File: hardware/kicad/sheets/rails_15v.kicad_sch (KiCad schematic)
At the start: 31 parts, among them U10 ADP7182AUJZ, U8 ADP5071AREZ, U9 ADP7142AUJZ

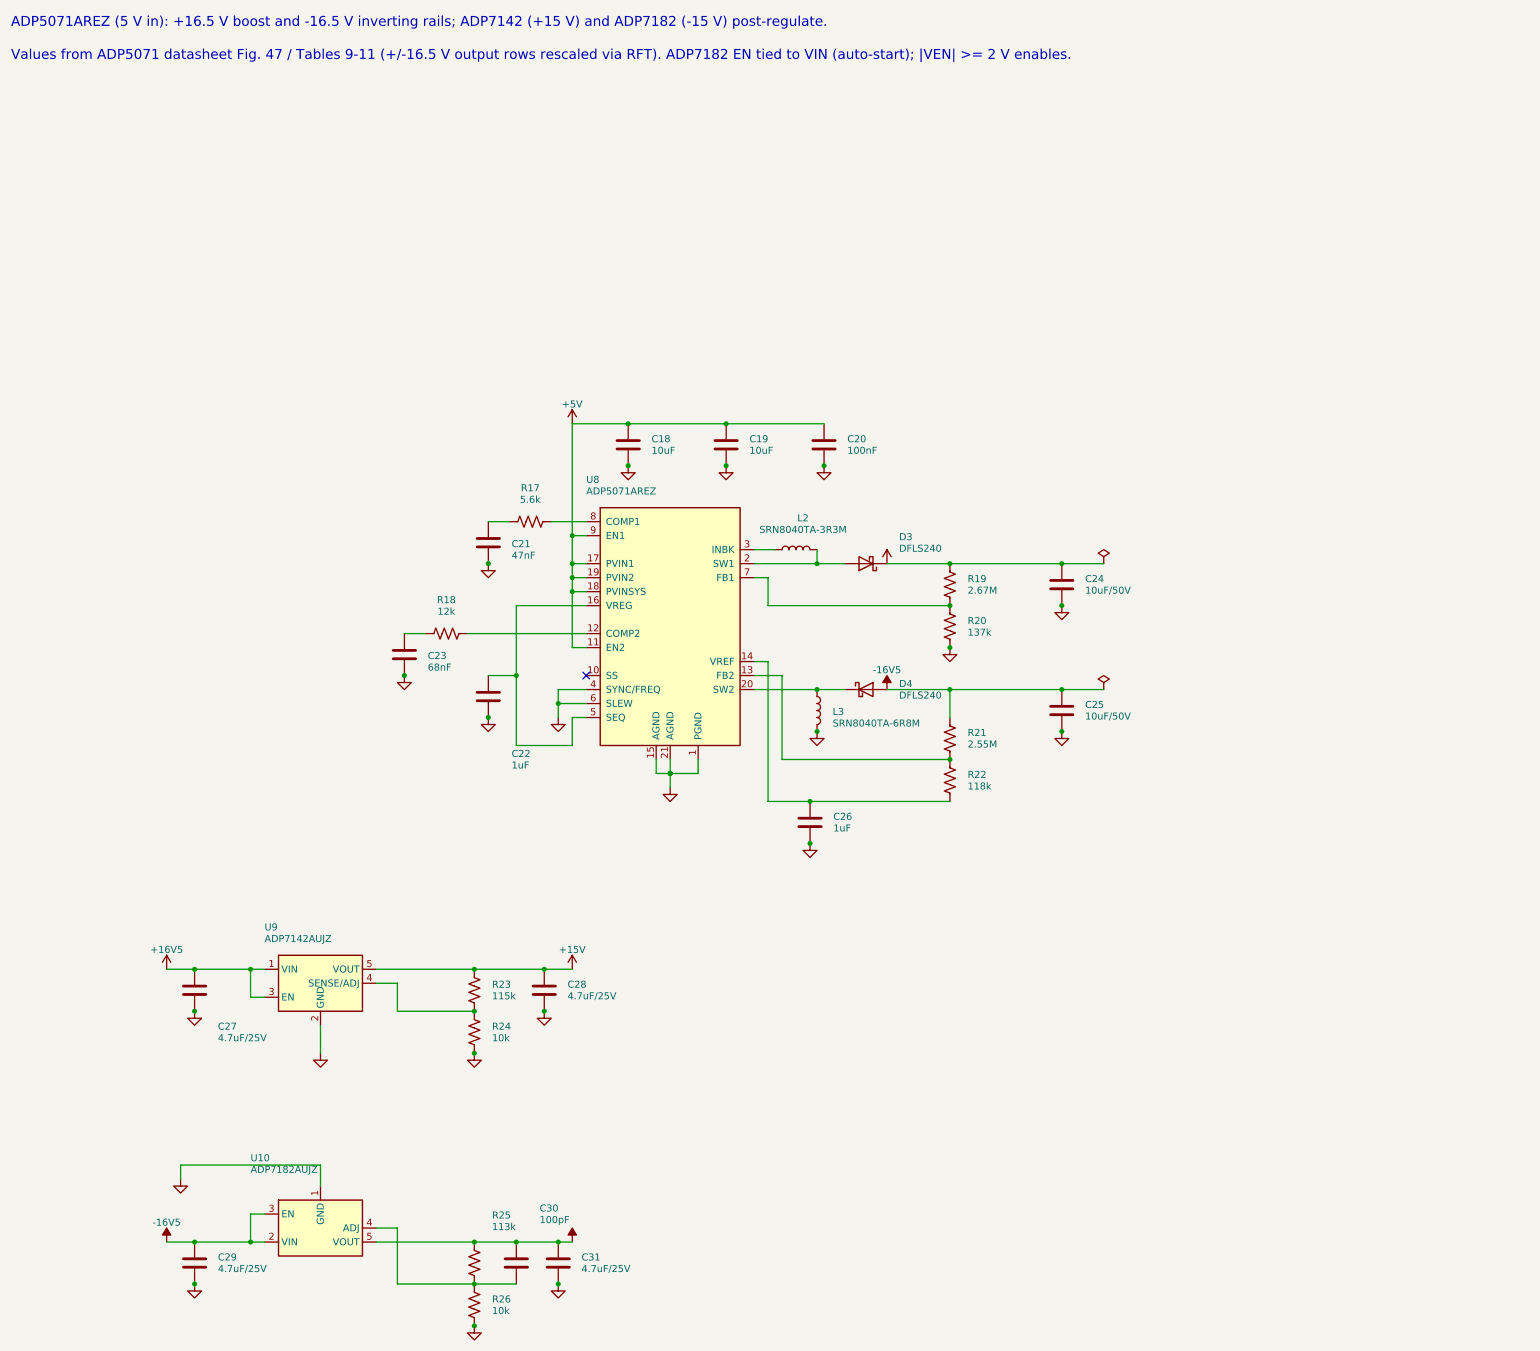
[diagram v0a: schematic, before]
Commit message: KiCad: cleaner layout, decoupling blocks, label directions, KiCad format fixes
- move IC decoupling caps into labelled blocks at the side of each sheet
- global labels show input/output direction per net
- no 4-way junctions (generator now checks and fails)
- generator output matches KiCad's saved format (hide property, junction
  and wire normalisation, lib symbol embedded fonts, multi-unit pins)
- hand-laid USB ESD protection as a pass-through

Co-Authored-By: Claude Sonnet 5.5 <noreply@anthropic.com>
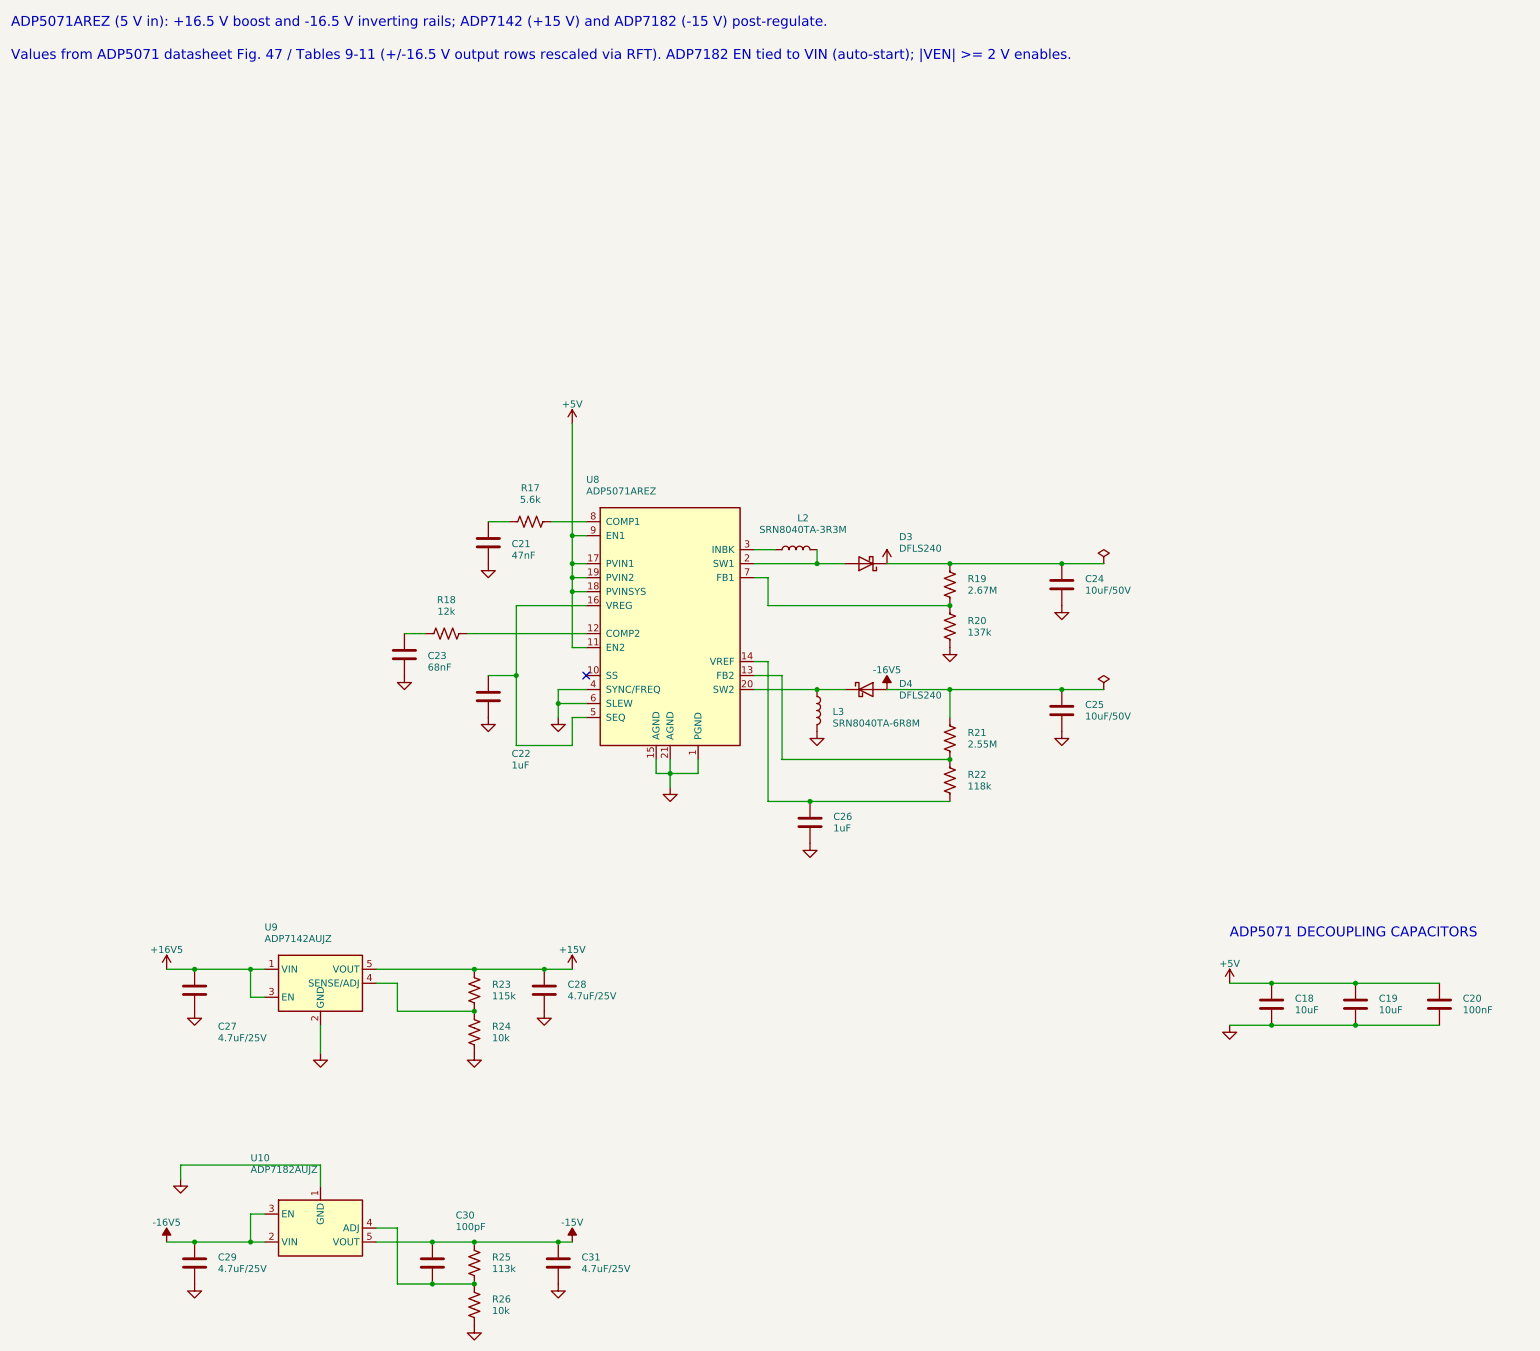
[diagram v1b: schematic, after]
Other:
- note added: "ADP5071 DECOUPLING CAPACITORS"
